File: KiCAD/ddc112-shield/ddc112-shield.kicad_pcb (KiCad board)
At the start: 2 copper layers, 68.6 x 53.3 mm, 8 parts, among them J1 Power, J2 Digital/PWM, J3 Analog, J4 Digital/PWM

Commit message: initial schematic; test software
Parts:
- added C1: 0.1uF, Capacitor_SMD:C_0805_2012Metric_Pad1.18x1.45mm_HandSolder, F.Cu at (138.7, 84.5)
- added C10: 10uF, Capacitor_SMD:C_0805_2012Metric_Pad1.18x1.45mm_HandSolder, F.Cu at (126.7, 59.4)
- added C11: 0.1uF, Capacitor_SMD:C_0805_2012Metric_Pad1.18x1.45mm_HandSolder, F.Cu at (129.2, 59.4)
- added C12: 0.33uF, Capacitor_SMD:C_0805_2012Metric_Pad1.18x1.45mm_HandSolder, F.Cu at (159.3, 91.1)
- added C13: 0.33uF, Capacitor_SMD:C_0805_2012Metric_Pad1.18x1.45mm_HandSolder, F.Cu at (116.1, 71.4)
- added C14: 0.1uF, Capacitor_SMD:C_0805_2012Metric_Pad1.18x1.45mm_HandSolder, F.Cu at (116.1, 62.5)
- added C2: 0.1uF, Capacitor_SMD:C_0805_2012Metric_Pad1.18x1.45mm_HandSolder, F.Cu at (150.2, 90.7)
- added C3: 10uF, Capacitor_SMD:C_0805_2012Metric_Pad1.18x1.45mm_HandSolder, F.Cu at (153.3, 90.7)
- added C4: 0.47uF, Capacitor_SMD:C_0805_2012Metric_Pad1.18x1.45mm_HandSolder, F.Cu at (138.7, 90.7)
- added C5: 10uF, Capacitor_SMD:C_0805_2012Metric_Pad1.18x1.45mm_HandSolder, F.Cu at (138.7, 77.1)
- added C6: 0.1uF, Capacitor_SMD:C_0805_2012Metric_Pad1.18x1.45mm_HandSolder, F.Cu at (141.3, 77.1)
- added C7: 0.1uF, Capacitor_SMD:C_0805_2012Metric_Pad1.18x1.45mm_HandSolder, F.Cu at (159.3, 82.2)
- added C8: 10uF, Capacitor_SMD:C_0805_2012Metric_Pad1.18x1.45mm_HandSolder, F.Cu at (141.9, 59.4)
- added C9: 0.1uF, Capacitor_SMD:C_0805_2012Metric_Pad1.18x1.45mm_HandSolder, F.Cu at (139.4, 59.4)
- added J5: Conn_01x02, Connector_PinHeader_2.54mm:PinHeader_1x02_P2.54mm_Vertical, F.Cu at (152.1, 63.2)
- added J6: Conn_01x02, Connector_PinHeader_2.54mm:PinHeader_1x02_P2.54mm_Vertical, F.Cu at (152.1, 73.3)
- added J7: Screw_Terminal_01x02, TerminalBlock:TerminalBlock_MaiXu_MX126-5.0-02P_1x02_P5.00mm, F.Cu at (105.1, 51.8)
- added R1: 10k, Resistor_SMD:R_0805_2012Metric_Pad1.20x1.40mm_HandSolder, F.Cu at (147.0, 90.7)
- added R2: 0R, Resistor_SMD:R_0805_2012Metric_Pad1.20x1.40mm_HandSolder, B.Cu at (137.5, 67.6)
- added U1: DDC112, Package_SO:SOIC-28W_7.5x17.9mm_P1.27mm, F.Cu at (137.5, 68.3)
- added U2: REF3040, Package_TO_SOT_SMD:SOT-23, F.Cu at (143.2, 90.7)
- added U3: OPA350, Package_SO:SOIC-8_3.9x4.9mm_P1.27mm, F.Cu at (144.4, 84.5)
- added U4: L78L05_SOT89, Package_TO_SOT_SMD:SOT-89-3, F.Cu at (159.9, 86.7)
- added U5: L78L05_SOT89, Package_TO_SOT_SMD:SOT-89-3, F.Cu at (116.7, 67.0)
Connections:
- net /*10 renamed /PB2/SS
- net /*11 renamed /PB3/MOSI
- net /*3 renamed /PD3
- net /12 renamed /PB4/MISO
- net /2 renamed /PD2
- net /4 renamed /PD4
- net /A3 renamed /PC3/ADC3
- net /RX/0 renamed /PD0/TXD
- net /SCL/A5 renamed /PC5/SCL/ADC5
- net /SDA/A4 renamed /PC4/SDA/ADC4
- net /TX/1 renamed /PD1/TXD
- net VCC renamed /Vin
- J2 pad 10: /8 -> /PB0
- J2 pad 5: /13 -> /PB5/SCLK
- J2 pad 9: /*9 -> /PB1/OC1A
- J3 pad 1: /A0 -> /PC0/ADC0
- J3 pad 2: /A1 -> /PC1/ADC1
- J3 pad 3: /A2 -> /PC2/ADC2
- J4 pad 1: /7 -> /PD7
- J4 pad 2: /*6 -> /PD6/OC0A
- J4 pad 3: /*5 -> /PD5
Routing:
- net /PC2/ADC2: track 0.00 -> 46.9 mm
- net /PC1/ADC1: track 0.00 -> 45.4 mm
- net /PC0/ADC0: track 0.00 -> 43.7 mm
- net /PD7: track 0.00 -> 34.6 mm
- net /PD6/OC0A: track 0.00 -> 25.3 mm
- net /PD5: track 0.00 -> 24.6 mm
- net /PB0: track 0.00 -> 22.3 mm
- net /PB1/OC1A: track 0.00 -> 15.9 mm, vias 0 -> 1
- net GND: track 0.00 -> 9.48 mm, vias 0 -> 5
- net Net-(J6-Pin_1): track 0.00 -> 6.53 mm
- net Net-(J5-Pin_1): track 0.00 -> 6.53 mm
- net Earth: track 0.00 -> 3.57 mm, vias 0 -> 2
- added copper zone on In1.Cu, net Earth
- added copper zone on In1.Cu, net GND
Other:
- copper layers 2 -> 4

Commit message: placement adjust
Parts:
- moved C12 8.50 mm to (163.5, 83.7), turned to 90 degrees
- moved C7 4.91 mm to (154.6, 83.7), turned to 90 degrees
- moved U4 3.68 mm to (159.1, 83.1), turned to 90 degrees
- moved C1 1.43 mm to (139.1, 83.2)
- moved C2 1.43 mm to (150.5, 89.3)
- moved C3 1.43 mm to (153.7, 89.3)
- moved C4 1.43 mm to (139.1, 89.3)
- moved R1 1.43 mm to (147.4, 89.3)
- moved U2 1.43 mm to (143.6, 89.3)
- moved U3 1.43 mm to (144.8, 83.2)

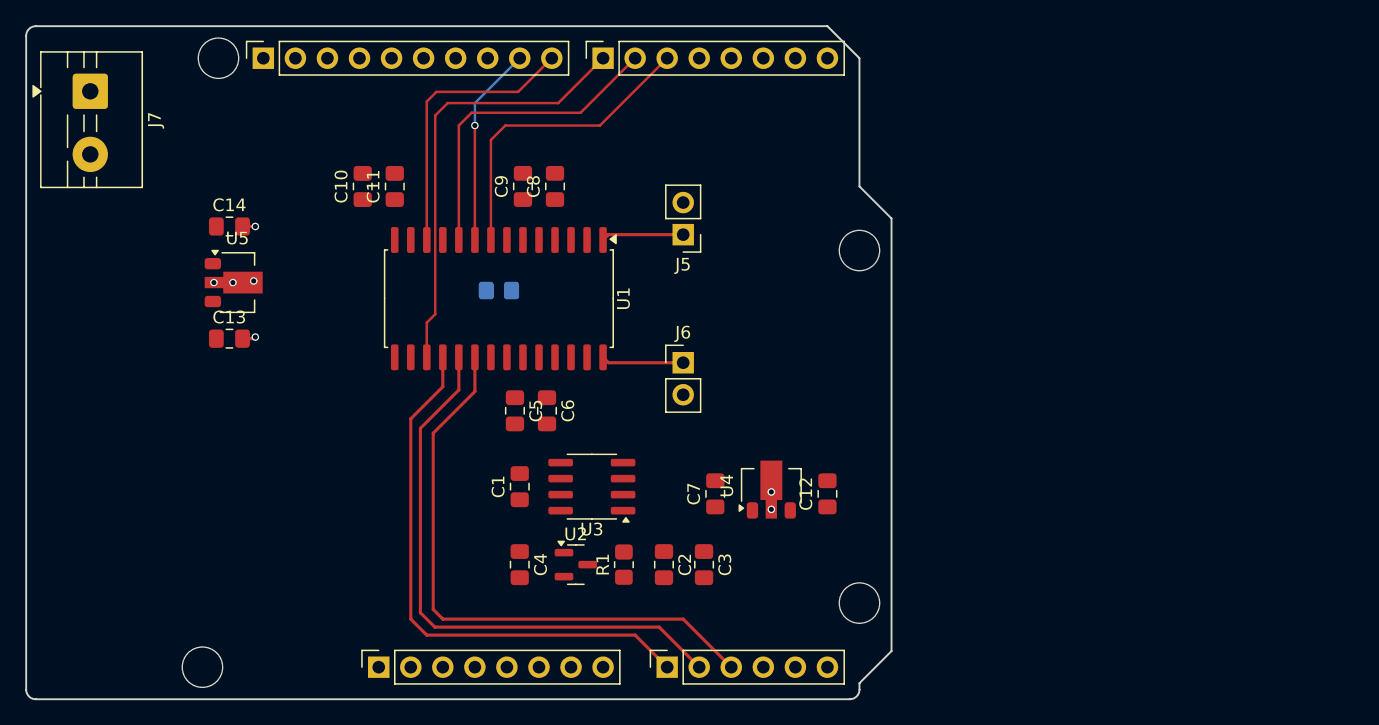
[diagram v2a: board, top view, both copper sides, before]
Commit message: starting on LED driver
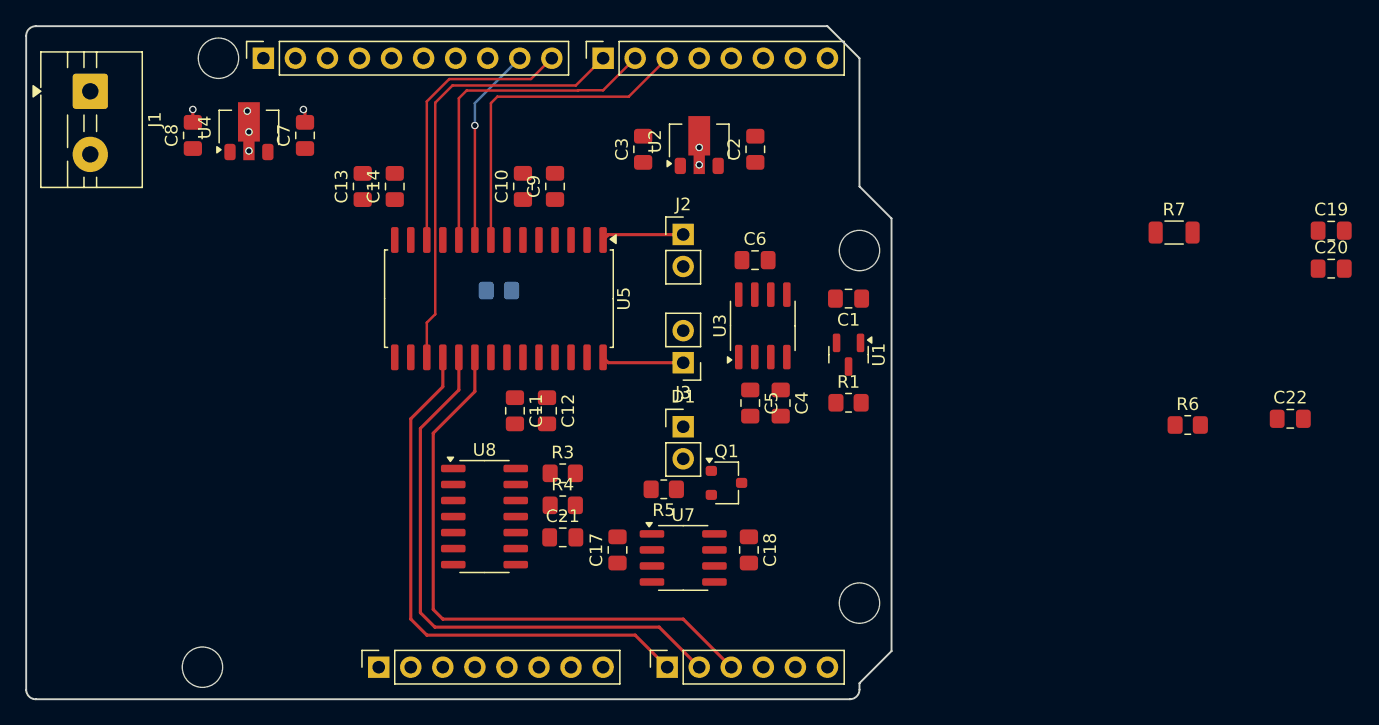
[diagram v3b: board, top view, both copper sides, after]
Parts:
- added C17: 120pF, Capacitor_SMD:C_0805_2012Metric_Pad1.18x1.45mm_HandSolder, F.Cu at (146.9, 88.2)
- added C18: 0.1uF, Capacitor_SMD:C_0805_2012Metric_Pad1.18x1.45mm_HandSolder, F.Cu at (157.3, 88.2)
- added C19: C, Capacitor_SMD:C_0805_2012Metric_Pad1.18x1.45mm_HandSolder, F.Cu at (203.4, 62.9)
- added C20: C, Capacitor_SMD:C_0805_2012Metric_Pad1.18x1.45mm_HandSolder, F.Cu at (203.4, 65.9)
- added C21: 0.1uF, Capacitor_SMD:C_0805_2012Metric_Pad1.18x1.45mm_HandSolder, F.Cu at (142.5, 87.2)
- added C22: 0.1uF, Capacitor_SMD:C_0805_2012Metric_Pad1.18x1.45mm_HandSolder, F.Cu at (200.2, 77.8)
- added D1: LED, Connector_PinHeader_2.54mm:PinHeader_1x02_P2.54mm_Vertical, F.Cu at (152.1, 78.4)
- added Q1: TTC1949, Package_TO_SOT_SMD:SC-59, F.Cu at (155.5, 82.9)
- added R3: 1k, Resistor_SMD:R_0805_2012Metric_Pad1.20x1.40mm_HandSolder, F.Cu at (142.5, 82.1)
- added R4: 1k, Resistor_SMD:R_0805_2012Metric_Pad1.20x1.40mm_HandSolder, F.Cu at (142.5, 84.6)
- added R5: 1k, Resistor_SMD:R_0805_2012Metric_Pad1.20x1.40mm_HandSolder, F.Cu at (150.5, 83.4)
- added R6: 1k, Resistor_SMD:R_0805_2012Metric_Pad1.20x1.40mm_HandSolder, F.Cu at (192.1, 78.3)
- added R7: 25, Resistor_SMD:R_1206_3216Metric, F.Cu at (191.0, 63.0)
- added U7: TLV272IS-13, Package_SO:SOIC-8_3.9x4.9mm_P1.27mm, F.Cu at (152.1, 88.8)
- added U8: MCP4922-EP, Package_SO:SOIC-14_3.9x8.7mm_P1.27mm, F.Cu at (136.3, 85.5)
- moved C1 33.5 mm to (165.2, 68.2), turned to 180 degrees
- moved U2 27.9 mm to (153.3, 55.8)
- moved C2 27.9 mm to (157.8, 56.4)
- moved C3 27.9 mm to (148.9, 56.4)
- moved U1 27.3 mm to (165.2, 72.7), turned to -90 degrees
- moved C6 25.9 mm to (157.8, 65.2), turned to 0 degrees
- moved R1 21.9 mm to (165.2, 76.5), turned to 0 degrees
- moved U3 18.6 mm to (158.4, 70.4), turned to 90 degrees
- moved C7 17.2 mm to (122.1, 55.3), turned to 90 degrees
- moved C5 14.5 mm to (157.4, 76.5)
- moved C4 14.2 mm to (159.8, 76.5)
- moved U4 12.3 mm to (117.7, 54.7), turned to 90 degrees
- moved C8 7.78 mm to (113.2, 55.3), turned to 90 degrees
- turned J2 to 0 degrees
- turned J3 to 180 degrees
- renumbered C4 to C1, C9 to C10, C5 to C11, C6 to C12, C10 to C13, C11 to C14, C12 to C2, C7 to C3, C3 to C4, C2 to C5, C1 to C6, C13 to C7, C14 to C8, C8 to C9, J7 to J1, J5 to J2, J6 to J3, J1 to J4, J3 to J5, J2 to J6, J4 to J7, U2 to U1, U4 to U2, U5 to U4, U1 to U5
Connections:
- U5 pad 24: unconnected-(U1-CAP2A-Pad24) -> Net-(C20-Pad1)
- U5 pad 25: unconnected-(U1-CAP2B-Pad25) -> Net-(C20-Pad2)
- U5 pad 4: unconnected-(U1-CAP1B-Pad4) -> Net-(C19-Pad2)
- U5 pad 5: unconnected-(U1-CAP1A-Pad5) -> Net-(C19-Pad1)
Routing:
- net /PD5: track 24.6 -> 26.3 mm
- net /PD6/OC0A: track 25.3 -> 26.5 mm
- net /PD7: track 34.6 -> 35.2 mm

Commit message: LED driver schematic complete?
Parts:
- removed U7: TLV272IS-13, Package_SO:SOIC-8_3.9x4.9mm_P1.27mm
- added C15: 0.33uF, Capacitor_SMD:C_0805_2012Metric_Pad1.18x1.45mm_HandSolder, F.Cu at (189.7, 82.4)
- added C16: 0.1uF, Capacitor_SMD:C_0805_2012Metric_Pad1.18x1.45mm_HandSolder, F.Cu at (189.7, 85.5)
- added D2: LED, Connector_PinHeader_2.54mm:PinHeader_1x02_P2.54mm_Vertical, F.Cu at (196.4, 83.2)
- added D3: LED, Connector_PinHeader_2.54mm:PinHeader_1x02_P2.54mm_Vertical, F.Cu at (201.0, 83.2)
- added Q2: TTC1949, Package_TO_SOT_SMD:SC-59, F.Cu at (176.4, 83.4)
- added Q3: TTC1949, Package_TO_SOT_SMD:SC-59, F.Cu at (176.4, 88.3)
- added Q4: TTC1949, Package_TO_SOT_SMD:SC-59, F.Cu at (176.4, 93.1)
- added R8: 4.7k, Resistor_SMD:R_0805_2012Metric_Pad1.20x1.40mm_HandSolder, F.Cu at (196.5, 89.5)
- added R9: 4.7k, Resistor_SMD:R_0805_2012Metric_Pad1.20x1.40mm_HandSolder, F.Cu at (196.5, 92.5)
- added U6: LTC1380, Package_SO:SOIC-16_3.9x9.9mm_P1.27mm, F.Cu at (183.1, 86.8)
- added U9: LTC2631, Package_TO_SOT_SMD:TSOT-23-8, F.Cu at (181.4, 94.9)
- C21: value 0.1uF -> 1nF
- R4: value 1k -> 440
- U8: value MCP4922-EP -> OPA365xxD; footprint Package_SO:SOIC-14_3.9x8.7mm_P1.27mm -> Package_SO:SOIC-8_3.9x4.9mm_P1.27mm
- moved U8 64.3 mm to (198.5, 69.1)
- moved C22 15.0 mm to (189.7, 88.5)
- moved C20 12.5 mm to (191.9, 60.9)
- moved C19 12.5 mm to (191.9, 57.9)
- moved R6 12.5 mm to (180.6, 73.3)
- moved R7 12.5 mm to (179.5, 58.0)
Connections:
- net /LED_driver/LED_A renamed /LED_driver/LED_1
- C17 pad 1: Net-(U7A--) -> Net-(U8--)
- C21 pad 1: Net-(U7A-+) -> Net-(U8-+)
- C22 pad 2: GND -> Earth
- Q1 pad 1: Net-(Q1-B) -> +5VA
- R3 pad 1: Net-(U7A-+) -> Net-(U8-+)
- R3 pad 2: Net-(U8-VoutA) -> Net-(U9-Vout)
- R4 pad 1: Net-(U7A-+) -> Net-(U8-+)
- R5 pad 1: Net-(Q1-B) -> Net-(U6-I/O)
- R6 pad 2: Net-(U7A--) -> Net-(U8--)
- U5 pad 13: /MOSI/11 -> /PB3/MOSI
- U5 pad 16: /MISO/12 -> /PB4/MISO
- U8 pad 1: +5VA -> unconnected-(U8-NC-Pad1)
- U8 pad 2: unconnected-(U8-NC-Pad2) -> Net-(U8--)
- U8 pad 3: /PD4 -> Net-(U8-+)
- U8 pad 4: /PB5/SCLK -> Earth
- U8 pad 5: /PB3/MOSI -> unconnected-(U8-NC-Pad5)
- U8 pad 6: unconnected-(U8-NC-Pad6) -> Net-(C17-Pad2)
- U8 pad 7: unconnected-(U8-NC-Pad7) -> +5VA
- U8 pad 8: GND -> unconnected-(U8-NC-Pad8)
